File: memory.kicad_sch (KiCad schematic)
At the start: 0 parts

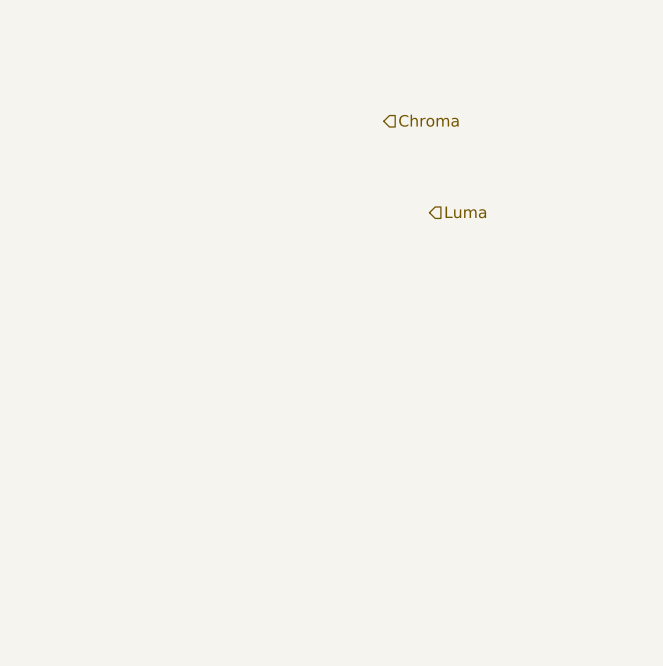
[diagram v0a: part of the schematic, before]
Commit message: continuing schematic capture, renamed sheets
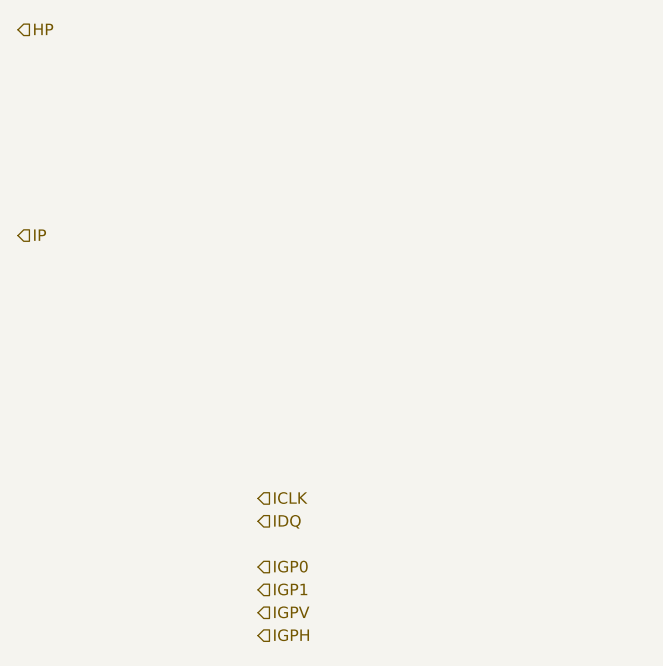
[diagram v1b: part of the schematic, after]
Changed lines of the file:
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@@
 (kicad_sch (version 20230121) (generator eeschema)
   (paper "A4")
+  (hierarchical_label "IGPV" (shape input) (at 83.82 109.22 0) (fields_autoplaced)
+    (effects (font (size 1.27 1.27)) (justify left))
+  )
+  (hierarchical_label "ICLK" (shape input) (at 83.82 96.52 0) (fields_autoplaced)
+    (effects (font (size 1.27 1.27)) (justify left))
+  )
+  (hierarchical_label "IGP1" (shape input) (at 83.82 106.68 0) (fields_autoplaced)
+    (effects (font (size 1.27 1.27)) (justify left))
+  )
   (hierarchical_label "Y" (shape output) (at 148.59 57.15 0) (fields_autoplaced)
     (effects (font (size 1.27 1.27)) (justify left))
   )
-  (hierarchical_label "Chroma" (shape input) (at 97.79 54.61 0) (fields_autoplaced)
+  (hierarchical_label "IDQ" (shape input) (at 83.82 99.06 0) (fields_autoplaced)
     (effects (font (size 1.27 1.27)) (justify left))
   )
-  (hierarchical_label "Luma" (shape input) (at 102.87 64.77 0) (fields_autoplaced)
+  (hierarchical_label "IGP0" (shape input) (at 83.82 104.14 0) (fields_autoplaced)
+    (effects (font (size 1.27 1.27)) (justify left))
+  )
+  (hierarchical_label "IP" (shape input) (at 57.15 67.31 0) (fields_autoplaced)
     (effects (font (size 1.27 1.27)) (justify left))
   )
@@
     (effects (font (size 1.27 1.27)) (justify left))
   )
+  (hierarchical_label "HP" (shape input) (at 57.15 44.45 0) (fields_autoplaced)
+    (effects (font (size 1.27 1.27)) (justify left))
+  )
+  (hierarchical_label "IGPH" (shape input) (at 83.82 111.76 0) (fields_autoplaced)
+    (effects (font (size 1.27 1.27)) (justify left))
+  )

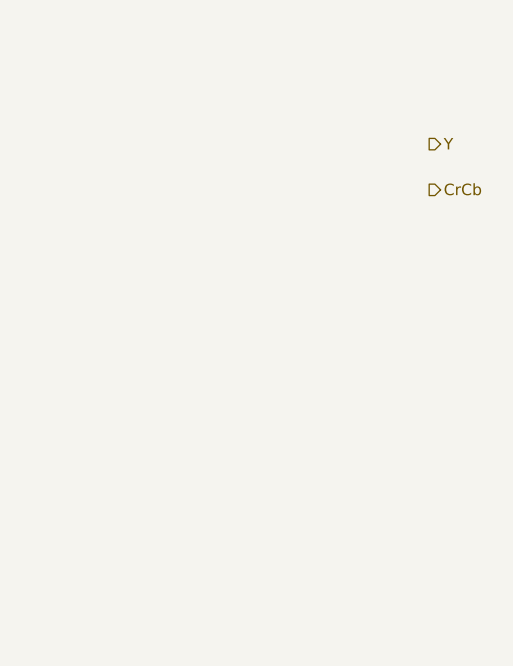
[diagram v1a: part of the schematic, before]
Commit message: added decoder symbol
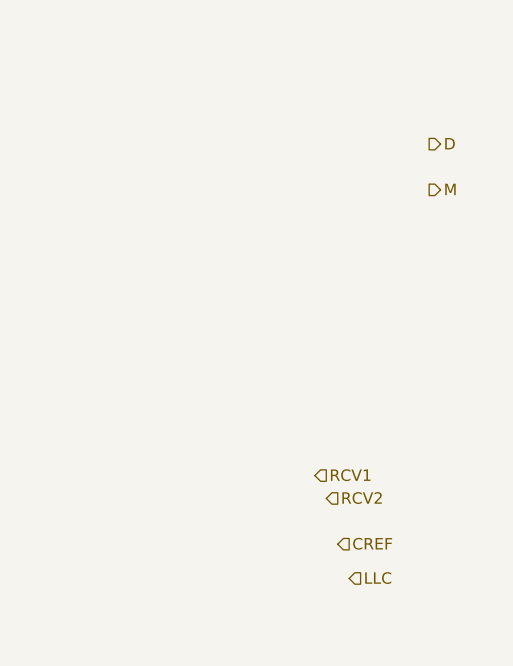
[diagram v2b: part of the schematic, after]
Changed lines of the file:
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@@
     (effects (font (size 1.27 1.27)) (justify left))
   )
-  (hierarchical_label "Y" (shape output) (at 148.59 57.15 0) (fields_autoplaced)
+  (hierarchical_label "CREF" (shape input) (at 138.43 101.6 0) (fields_autoplaced)
+    (effects (font (size 1.27 1.27)) (justify left))
+  )
+  (hierarchical_label "LLC" (shape input) (at 139.7 105.41 0) (fields_autoplaced)
+    (effects (font (size 1.27 1.27)) (justify left))
+  )
+  (hierarchical_label "D" (shape output) (at 148.59 57.15 0) (fields_autoplaced)
+    (effects (font (size 1.27 1.27)) (justify left))
+  )
+  (hierarchical_label "RCV1" (shape input) (at 135.89 93.98 0) (fields_autoplaced)
     (effects (font (size 1.27 1.27)) (justify left))
   )
@@
     (effects (font (size 1.27 1.27)) (justify left))
   )
+  (hierarchical_label "RCV2" (shape input) (at 137.16 96.52 0) (fields_autoplaced)
+    (effects (font (size 1.27 1.27)) (justify left))
+  )
   (hierarchical_label "IP" (shape input) (at 57.15 67.31 0) (fields_autoplaced)
     (effects (font (size 1.27 1.27)) (justify left))
   )
-  (hierarchical_label "CrCb" (shape output) (at 148.59 62.23 0) (fields_autoplaced)
+  (hierarchical_label "M" (shape output) (at 148.59 62.23 0) (fields_autoplaced)
     (effects (font (size 1.27 1.27)) (justify left))
   )

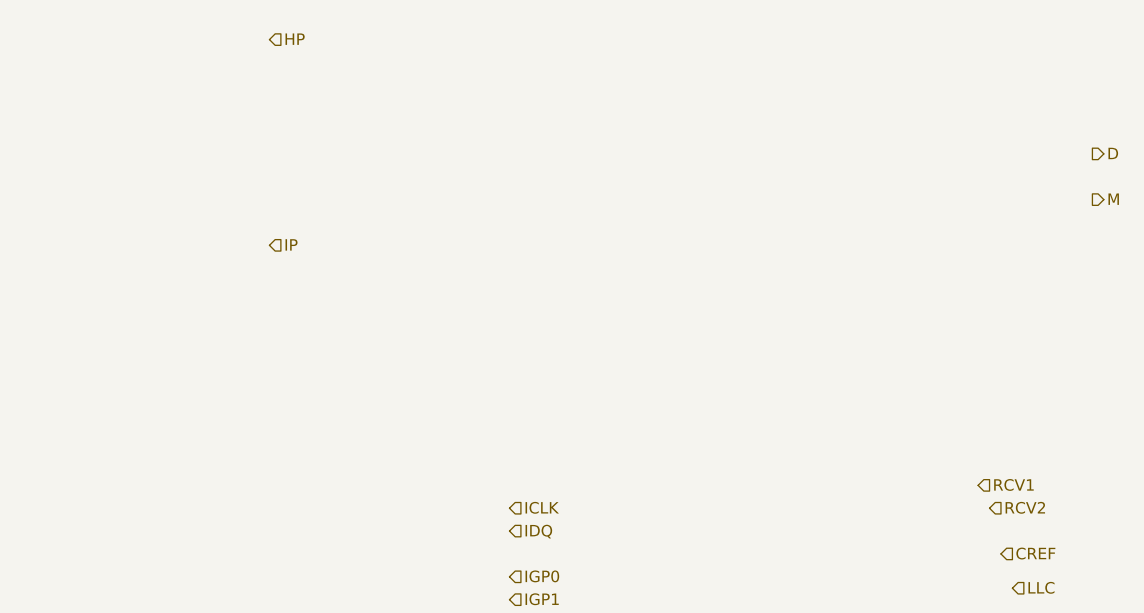
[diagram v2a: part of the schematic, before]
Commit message: added buses, title block info
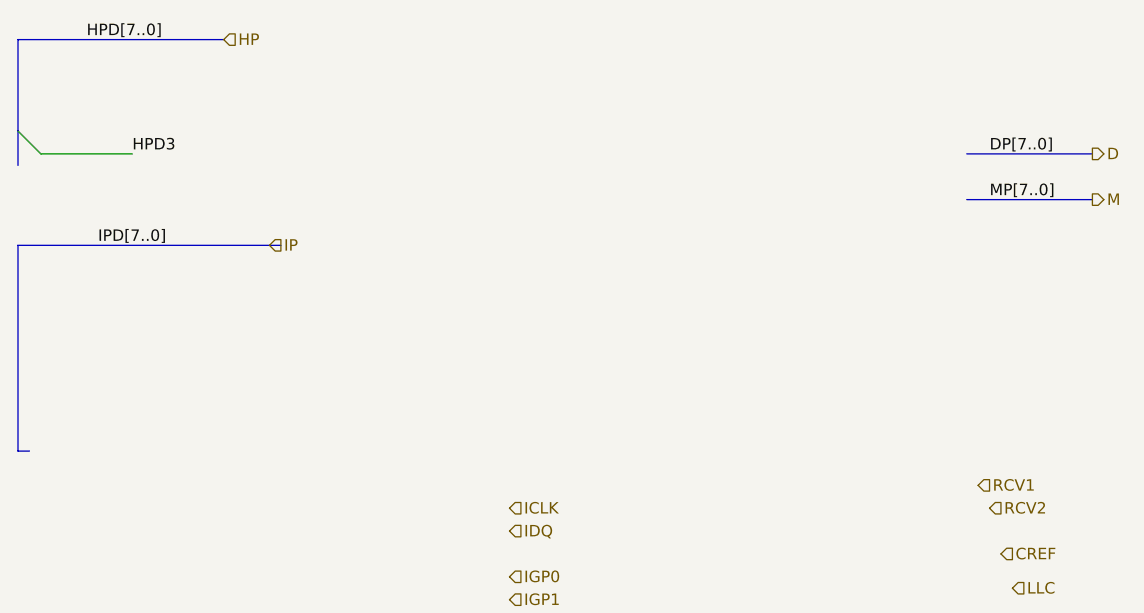
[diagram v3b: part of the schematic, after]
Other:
- title: (none) -> Time Base Corrector and Video Scaler
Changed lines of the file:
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@@
 (kicad_sch (version 20230121) (generator eeschema)
-  (paper "A4")
+  (paper "A4" portrait)
+  (title_block
+    (title "Time Base Corrector and Video Scaler")
+    (date "2024-01-15")
+    (rev "1")
+  )
+  (bus_entry (at 29.21 54.61) (size 2.54 2.54)
+    (stroke (width 0) (type default))
+  )
+  (bus (pts (xy 29.21 90.17) (xy 30.48 90.17))
+    (stroke (width 0) (type default))
+  )
+  (bus (pts (xy 134.62 57.15) (xy 148.59 57.15))
+    (stroke (width 0) (type default))
+  )
+  (wire (pts (xy 31.75 57.15) (xy 41.91 57.15))
+    (stroke (width 0) (type default))
+  )
+  (bus (pts (xy 52.07 44.45) (xy 29.21 44.45))
+    (stroke (width 0) (type default))
+  )
+  (bus (pts (xy 29.21 54.61) (xy 29.21 58.42))
+    (stroke (width 0) (type default))
+  )
+  (bus (pts (xy 58.42 67.31) (xy 29.21 67.31))
+    (stroke (width 0) (type default))
+  )
+  (bus (pts (xy 29.21 67.31) (xy 29.21 90.17))
+    (stroke (width 0) (type default))
+  )
+  (bus (pts (xy 134.62 62.23) (xy 148.59 62.23))
+    (stroke (width 0) (type default))
+  )
+  (bus (pts (xy 29.21 44.45) (xy 29.21 54.61))
+    (stroke (width 0) (type default))
+  )
+  (label "HPD3" (at 41.91 57.15 0)
+    (effects (font (size 1.27 1.27)) (justify left bottom))
+  )
+  (label "IPD[7..0]" (at 38.1 67.31 0) (fields_autoplaced)
+    (effects (font (size 1.27 1.27)) (justify left bottom))
+  )
+  (label "HPD[7..0]" (at 36.83 44.45 0) (fields_autoplaced)
+    (effects (font (size 1.27 1.27)) (justify left bottom))
+  )
+  (label "MP[7..0]" (at 137.16 62.23 0) (fields_autoplaced)
+    (effects (font (size 1.27 1.27)) (justify left bottom))
+  )
+  (label "DP[7..0]" (at 137.16 57.15 0) (fields_autoplaced)
+    (effects (font (size 1.27 1.27)) (justify left bottom))
+  )
   (hierarchical_label "IGPV" (shape input) (at 83.82 109.22 0) (fields_autoplaced)
     (effects (font (size 1.27 1.27)) (justify left))
@@
     (effects (font (size 1.27 1.27)) (justify left))
   )
-  (hierarchical_label "HP" (shape input) (at 57.15 44.45 0) (fields_autoplaced)
+  (hierarchical_label "HP" (shape input) (at 52.07 44.45 0) (fields_autoplaced)
     (effects (font (size 1.27 1.27)) (justify left))
   )

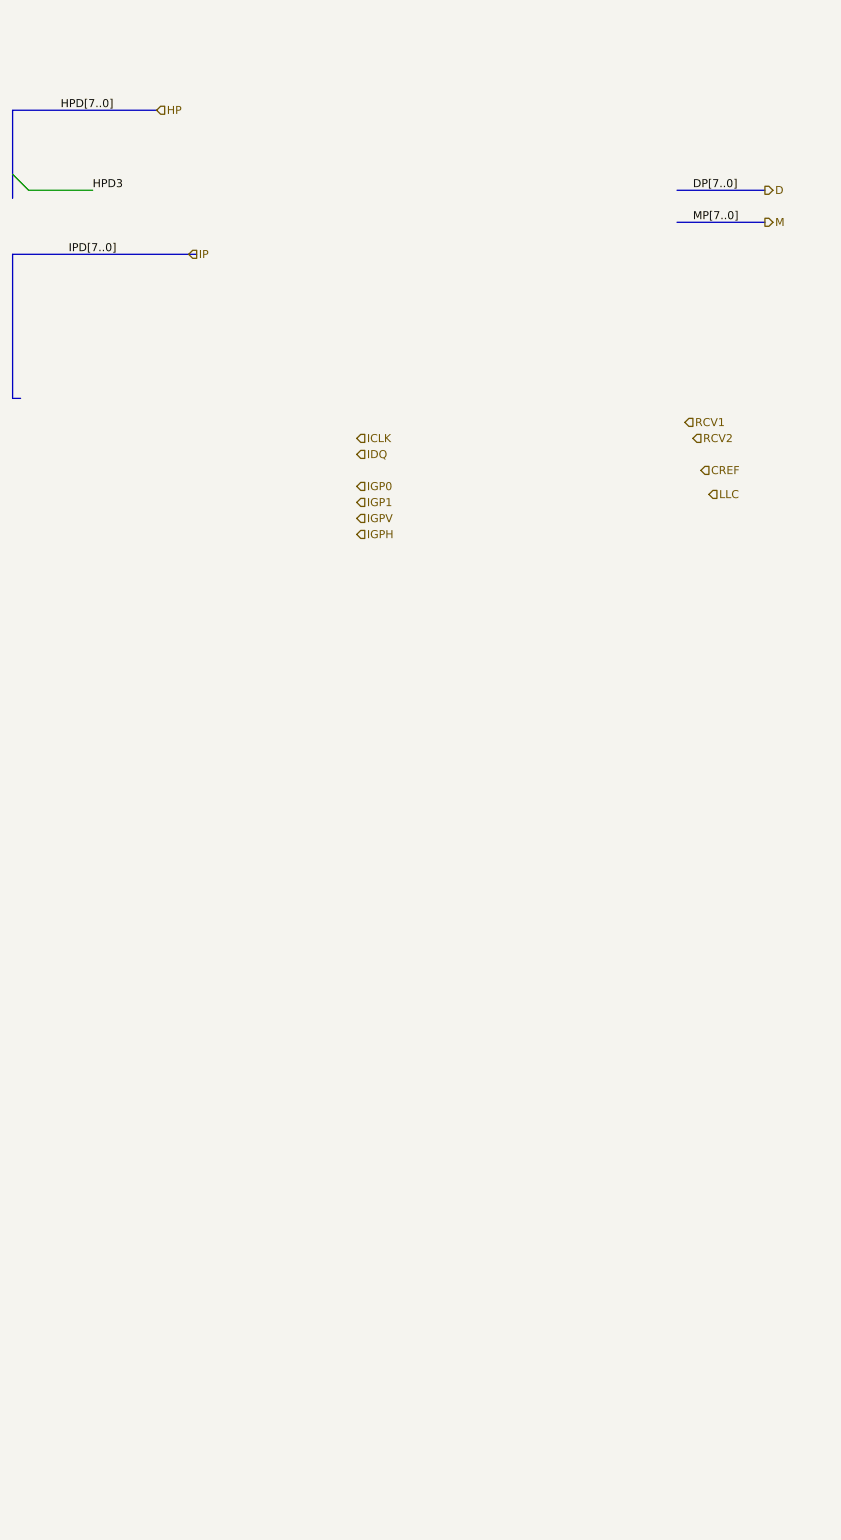
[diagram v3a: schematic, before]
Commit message: added frame memory symbol and updated schematic
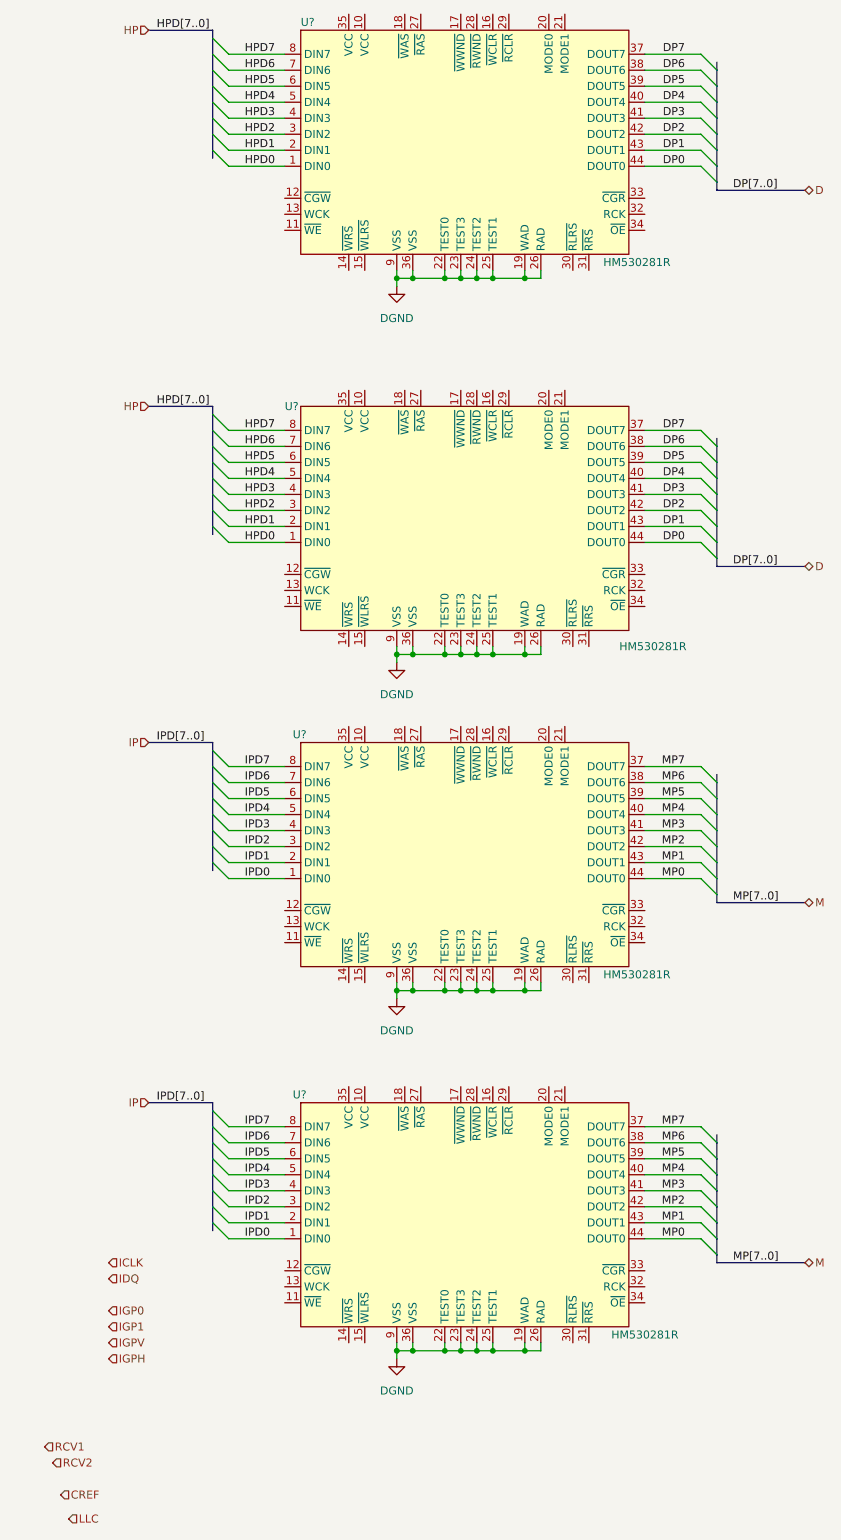
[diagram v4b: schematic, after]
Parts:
- added U? (x4): HM530281R, symbol tbc:HM530281R
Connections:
- net HPD3: now also U?.4 (DIN3), U?.4 (DIN3)
- new net DGND: U?.19 (WAD), U?.19 (WAD), U?.19 (WAD), U?.19 (WAD), U?.22 (TEST0), U?.22 (TEST0), U?.22 (TEST0), U?.22 (TEST0), U?.23 (TEST3), U?.23 (TEST3), U?.23 (TEST3), U?.23 (TEST3), U?.24 (TEST2), U?.24 (TEST2), U?.24 (TEST2), U?.24 (TEST2), U?.25 (TEST1), U?.25 (TEST1), U?.25 (TEST1), U?.25 (TEST1), U?.26 (RAD), U?.26 (RAD), U?.26 (RAD), U?.26 (RAD), U?.36 (VSS), U?.36 (VSS), U?.36 (VSS), U?.36 (VSS), U?.9 (VSS), U?.9 (VSS), U?.9 (VSS), U?.9 (VSS)
- new net DP0: U?.44 (DOUT0), U?.44 (DOUT0)
- new net DP1: U?.43 (DOUT1), U?.43 (DOUT1)
- new net DP2: U?.42 (DOUT2), U?.42 (DOUT2)
- new net DP3: U?.41 (DOUT3), U?.41 (DOUT3)
- new net DP4: U?.40 (DOUT4), U?.40 (DOUT4)
- new net DP5: U?.39 (DOUT5), U?.39 (DOUT5)
- new net DP6: U?.38 (DOUT6), U?.38 (DOUT6)
- new net DP7: U?.37 (DOUT7), U?.37 (DOUT7)
- new net HPD0: U?.1 (DIN0), U?.1 (DIN0)
- new net HPD1: U?.2 (DIN1), U?.2 (DIN1)
- new net HPD2: U?.3 (DIN2), U?.3 (DIN2)
- new net HPD4: U?.5 (DIN4), U?.5 (DIN4)
- new net HPD5: U?.6 (DIN5), U?.6 (DIN5)
- new net HPD6: U?.7 (DIN6), U?.7 (DIN6)
- new net HPD7: U?.8 (DIN7), U?.8 (DIN7)
- new net IPD0: U?.1 (DIN0), U?.1 (DIN0)
- new net IPD1: U?.2 (DIN1), U?.2 (DIN1)
- new net IPD2: U?.3 (DIN2), U?.3 (DIN2)
- new net IPD3: U?.4 (DIN3), U?.4 (DIN3)
- new net IPD4: U?.5 (DIN4), U?.5 (DIN4)
- new net IPD5: U?.6 (DIN5), U?.6 (DIN5)
- new net IPD6: U?.7 (DIN6), U?.7 (DIN6)
- new net IPD7: U?.8 (DIN7), U?.8 (DIN7)
- new net MP0: U?.44 (DOUT0), U?.44 (DOUT0)
- new net MP1: U?.43 (DOUT1), U?.43 (DOUT1)
- new net MP2: U?.42 (DOUT2), U?.42 (DOUT2)
- new net MP3: U?.41 (DOUT3), U?.41 (DOUT3)
- new net MP4: U?.40 (DOUT4), U?.40 (DOUT4)
- new net MP5: U?.39 (DOUT5), U?.39 (DOUT5)
- new net MP6: U?.38 (DOUT6), U?.38 (DOUT6)
- new net MP7: U?.37 (DOUT7), U?.37 (DOUT7)
